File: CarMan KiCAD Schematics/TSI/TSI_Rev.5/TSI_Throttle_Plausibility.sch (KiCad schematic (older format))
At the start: 64 parts, among them Q2 MMBF170, SW1 TS5A3159DBVT, U16 TS372CDT, U18 MCP6004, U22 MCP23016-I_SO, U23 DAC5574IDGS, U3 TS912, U30 TLP293, U6 TS912, U7 MCP6004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

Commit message: TSI (~97%)
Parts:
- renumbered TP1 to APPS1_ISO1, TP2 to APPS1_b1, TP3 to APPS2_b1, TP9 to APPS_DIFF1
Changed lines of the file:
@@
 	2250 4250 2250 4550
 $Comp
-L Connector:TestPoint TP1
+L Connector:TestPoint APPS1_ISO1
 U 1 1 613A1566
 P 2250 4250
-F 0 "TP1" H 2308 4368 50  0000 L CNN
+F 0 "APPS1_ISO1" H 2308 4368 50  0000 L CNN
 F 1 "APPS1_ISO" H 2308 4277 50  0000 L CNN
 F 2 "TestPoint:TestPoint_Pad_D3.0mm" H 2450 4250 50  0001 C CNN
@@
 	6400 10350 6400 10150
 $Comp
-L Connector:TestPoint TP3
+L Connector:TestPoint APPS2_b1
 U 1 1 601142BC
 P 6400 10150
-F 0 "TP3" H 6458 10268 50  0000 L CNN
+F 0 "APPS2_b1" H 6458 10268 50  0000 L CNN
 F 1 "APPS2_b" H 6458 10177 50  0000 L CNN
 F 2 "TestPoint:TestPoint_Pad_D3.0mm" H 6600 10150 50  0001 C CNN
@@
 	3000 10350 3000 10150
 $Comp
-L Connector:TestPoint TP2
+L Connector:TestPoint APPS1_b1
 U 1 1 600FB539
 P 3000 10150
-F 0 "TP2" H 3058 10268 50  0000 L CNN
+F 0 "APPS1_b1" H 3058 10268 50  0000 L CNN
 F 1 "APPS1_b" H 3058 10177 50  0000 L CNN
 F 2 "TestPoint:TestPoint_Pad_D3.0mm" H 3200 10150 50  0001 C CNN
@@
 10V
 $Comp
-L Connector:TestPoint TP9
+L Connector:TestPoint APPS_DIFF1
 U 1 1 6003107E
 P 5400 1950
-F 0 "TP9" H 5200 2150 50  0000 L CNN
+F 0 "APPS_DIFF1" H 5200 2150 50  0000 L CNN
 F 1 "APPS_DIFF" H 5458 1977 50  0001 L CNN
 F 2 "TestPoint:TestPoint_Pad_D3.0mm" H 5600 1950 50  0001 C CNN

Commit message: TSI (~98.5%)
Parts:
- renumbered APPS1_ISO1 to TP1, APPS_DIFF1 to TP2, APPS1_b1 to TP3, APPS2_b1 to TP9
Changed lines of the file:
@@
 	2250 4250 2250 4550
 $Comp
-L Connector:TestPoint APPS1_ISO1
+L Connector:TestPoint TP1
 U 1 1 613A1566
 P 2250 4250
-F 0 "APPS1_ISO1" H 2308 4368 50  0000 L CNN
+F 0 "TP1" H 2308 4368 50  0000 L CNN
 F 1 "APPS1_ISO" H 2308 4277 50  0000 L CNN
 F 2 "TestPoint:TestPoint_Pad_D3.0mm" H 2450 4250 50  0001 C CNN
@@
 	6400 10350 6400 10150
 $Comp
-L Connector:TestPoint APPS2_b1
+L Connector:TestPoint TP9
 U 1 1 601142BC
 P 6400 10150
-F 0 "APPS2_b1" H 6458 10268 50  0000 L CNN
+F 0 "TP9" H 6458 10268 50  0000 L CNN
 F 1 "APPS2_b" H 6458 10177 50  0000 L CNN
 F 2 "TestPoint:TestPoint_Pad_D3.0mm" H 6600 10150 50  0001 C CNN
@@
 	3000 10350 3000 10150
 $Comp
-L Connector:TestPoint APPS1_b1
+L Connector:TestPoint TP3
 U 1 1 600FB539
 P 3000 10150
-F 0 "APPS1_b1" H 3058 10268 50  0000 L CNN
+F 0 "TP3" H 3058 10268 50  0000 L CNN
 F 1 "APPS1_b" H 3058 10177 50  0000 L CNN
 F 2 "TestPoint:TestPoint_Pad_D3.0mm" H 3200 10150 50  0001 C CNN
@@
 10V
 $Comp
-L Connector:TestPoint APPS_DIFF1
+L Connector:TestPoint TP2
 U 1 1 6003107E
 P 5400 1950
-F 0 "APPS_DIFF1" H 5200 2150 50  0000 L CNN
+F 0 "TP2" H 5350 2150 50  0000 L CNN
 F 1 "APPS_DIFF" H 5458 1977 50  0001 L CNN
 F 2 "TestPoint:TestPoint_Pad_D3.0mm" H 5600 1950 50  0001 C CNN

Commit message: Aesthetics
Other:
- note added: "*Need 1% tolerance for R17 & R18*\n"
- note removed: "*Need 1% tolerance for R27 & R28*\n"
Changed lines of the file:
@@
 Connection ~ 2150 6850
 Text Notes 1000 8150 0    50   ~ 0
-*Need 1% tolerance for R27 & R28*\n
+*Need 1% tolerance for R17 & R18*\n
 Text Label 2350 6850 0    50   ~ 0
 5V_REF

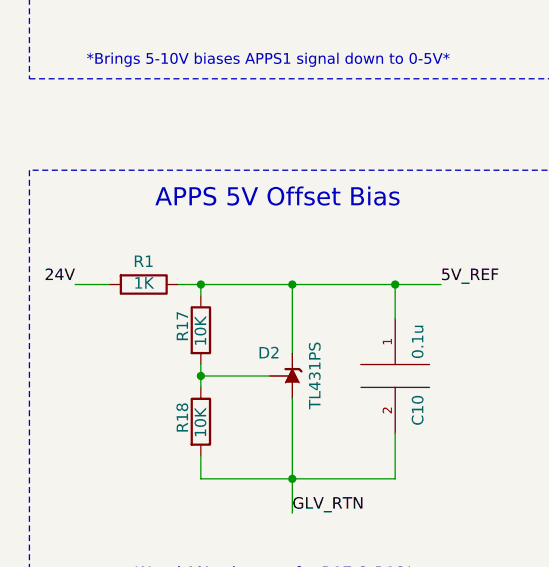
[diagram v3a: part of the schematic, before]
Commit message: Updated board, added silk art
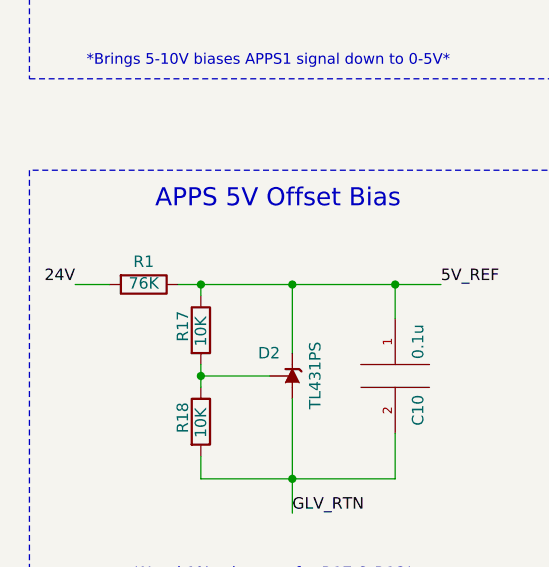
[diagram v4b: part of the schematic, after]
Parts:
- R1: value 1K -> 76K
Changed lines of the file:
@@
 P 1050 6850
 F 0 "R1" V 950 6850 50  0000 C CNN
-F 1 "1K" V 1074 6850 50  0000 C BNN
+F 1 "76K" V 1074 6850 50  0000 C BNN
 F 2 "Resistor_SMD:R_0805_2012Metric_Pad1.15x1.40mm_HandSolder" V 980 6850 50  0001 C CNN
 F 3 "~" H 1050 6850 50  0001 C CNN

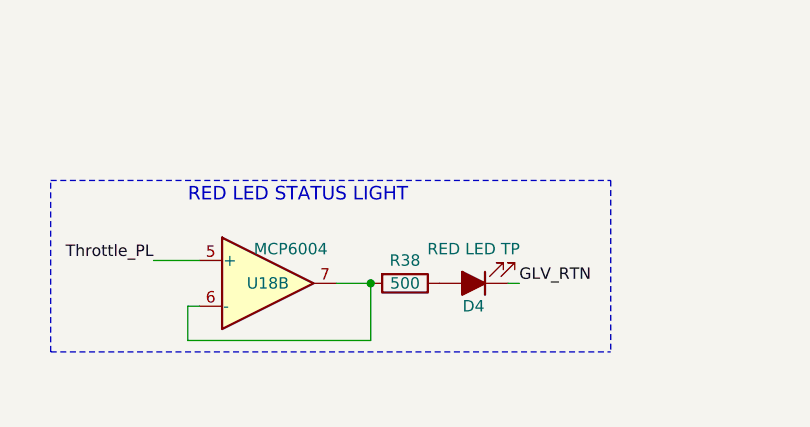
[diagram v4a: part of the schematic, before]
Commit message: Updated component links
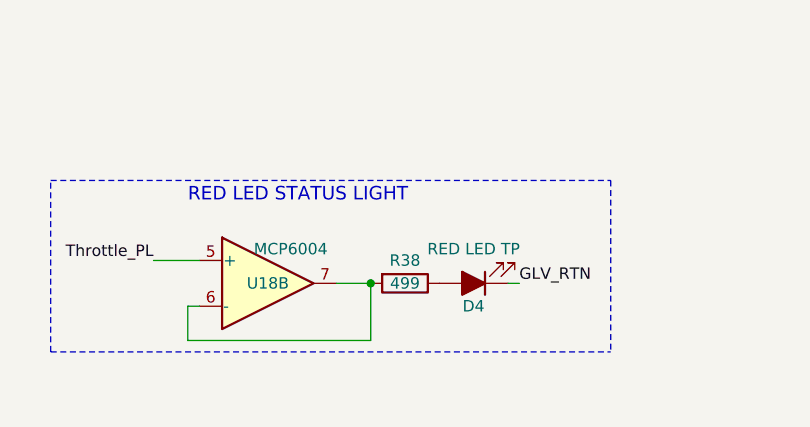
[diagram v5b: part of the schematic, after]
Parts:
- R38: value 500 -> 499
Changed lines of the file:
@@
 P 10000 10550
 F 0 "R38" V 9900 10550 50  0000 C CNN
-F 1 "500" V 10000 10550 50  0000 C CNN
+F 1 "499" V 10000 10550 50  0000 C CNN
 F 2 "Resistor_SMD:R_0805_2012Metric_Pad1.15x1.40mm_HandSolder" V 9930 10550 50  0001 C CNN
 F 3 "~" H 10000 10550 50  0001 C CNN

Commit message: Changed RV4 and RV5 footprint
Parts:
- RV4: footprint TSI_Rev_2021_Footprint_Lib:trim_pot -> TSI_Rev_2021_Footprint_Lib:Potentiometer
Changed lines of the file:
@@
 F 0 "RV4" H 5830 2246 50  0000 R CNN
 F 1 "1K" H 5830 2155 50  0000 R CNN
-F 2 "TSI_Rev_2021_Footprint_Lib:trim_pot" H 5900 2200 50  0001 C CNN
+F 2 "TSI_Rev_2021_Footprint_Lib:Potentiometer" H 5900 2200 50  0001 C CNN
 F 3 "~" H 5900 2200 50  0001 C CNN
 	1    5900 2200

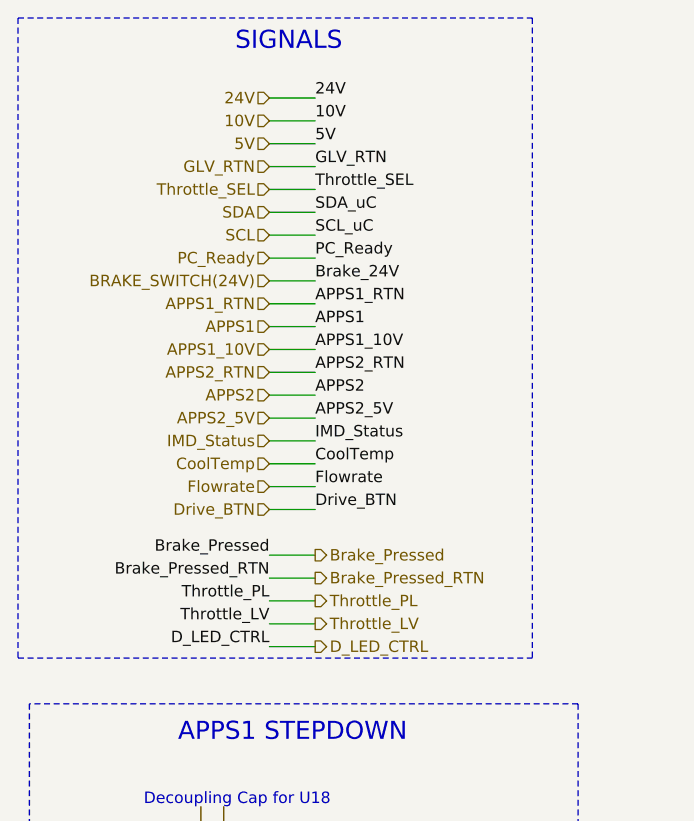
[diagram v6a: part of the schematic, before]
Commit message: TSI Signal Review ISSUES: - PCDC 'Pre_Charge_Ready' and 'PC_Ready' discrepancy - TSI Rev.4 IC1, IC4 -> PCDC & Isolators
REMOVED SIGNALS:
Throttle Plausibility
 - PC_Ready
 - Drive_BTN
 PCDC
 - HV+
 - HV-
 - Throttle_HV
 - IGNI_GND

STATUS LIGHTS & COCKPIT
- BP
- BP_RTN
- IMD_Status
- 5V
- Fault_LED
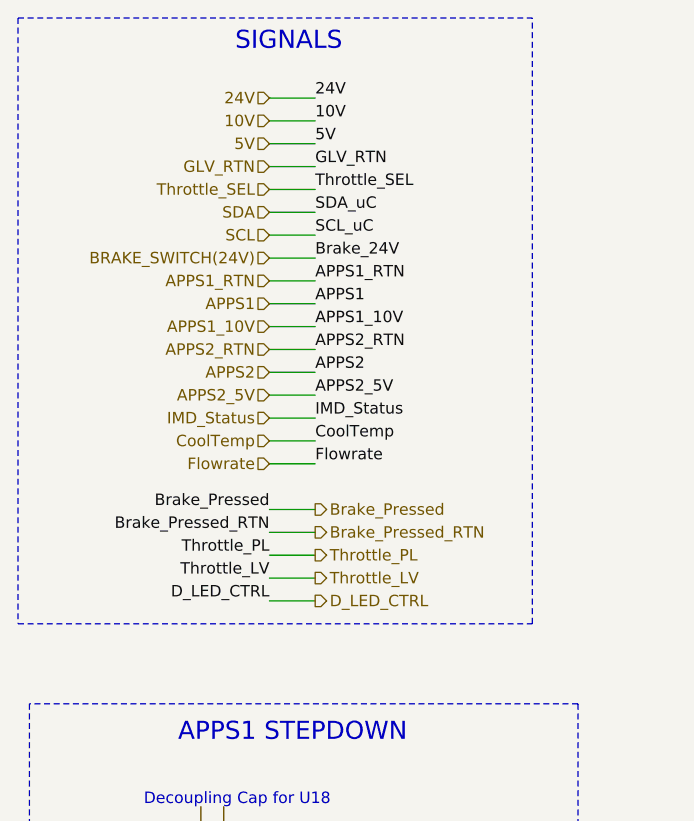
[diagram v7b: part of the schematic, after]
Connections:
- net labels removed: Drive_BTN, PC_Ready
- wire segments 288 -> 286
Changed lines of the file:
@@
 $Descr A3 16535 11693
 encoding utf-8
-Sheet 3 6
+Sheet 6 6
 Title ""
 Date ""
@@
 Text HLabel 1600 1450 0    50   Input ~ 0
 SCL
-Text HLabel 1600 1550 0    50   Input ~ 0
-PC_Ready
 Text Notes 1450 650  0    79   ~ 0
 SIGNALS\n
@@
 Text Label 1800 1050 0    50   ~ 0
 5V
-Wire Wire Line
-	1800 1550 1600 1550
-Text Label 1800 1550 0    50   ~ 0
-PC_Ready
 Wire Wire Line
 	2250 4250 2250 4550
@@
 Wire Wire Line
 	4100 2250 4250 2250
+Text Label 1800 1650 0    50   ~ 0
+APPS1_RTN
 Text Label 1800 1750 0    50   ~ 0
-APPS1_RTN
+APPS1
 Text Label 1800 1850 0    50   ~ 0
-APPS1
-Text Label 1800 1950 0    50   ~ 0
 APPS1_10V
+Text Label 1600 2750 2    50   ~ 0
+Brake_Pressed_RTN
+Text Label 1600 2650 2    50   ~ 0
+Brake_Pressed
+Wire Wire Line
+	1600 2750 1800 2750
+Wire Wire Line
+	1600 2650 1800 2650
 Text Label 1600 2950 2    50   ~ 0
+Throttle_LV
+Text Label 1600 2850 2    50   ~ 0
+Throttle_PL
+Wire Wire Line
+	1600 2950 1800 2950
+Wire Wire Line
+	1600 2850 1800 2850
+Text Label 1800 2050 0    50   ~ 0
+APPS2
+Text HLabel 1800 2850 2    50   Output ~ 0
+Throttle_PL
+Text HLabel 1800 2950 2    50   Output ~ 0
+Throttle_LV
+Text HLabel 1800 2750 2    50   Output ~ 0
 Brake_Pressed_RTN
-Text Label 1600 2850 2    50   ~ 0
-Brake_Pressed
-Wire Wire Line
-	1600 2950 1800 2950
-Wire Wire Line
-	1600 2850 1800 2850
-Text Label 1600 3150 2    50   ~ 0
-Throttle_LV
-Text Label 1600 3050 2    50   ~ 0
-Throttle_PL
-Wire Wire Line
-	1600 3150 1800 3150
-Wire Wire Line
-	1600 3050 1800 3050
-Text Label 1800 2150 0    50   ~ 0
-APPS2
-Text HLabel 1800 3050 2    50   Output ~ 0
-Throttle_PL
-Text HLabel 1800 3150 2    50   Output ~ 0
-Throttle_LV
-Text HLabel 1800 2950 2    50   Output ~ 0
-Brake_Pressed_RTN
-Text HLabel 1800 2850 2    50   Output ~ 0
+Text HLabel 1800 2650 2    50   Output ~ 0
 Brake_Pressed
 Wire Wire Line
@@
 Text Label 13050 8750 2    50   ~ 0
 24V
+Text HLabel 1600 1550 0    50   Input ~ 0
+BRAKE_SWITCH(24V)
+Text HLabel 1600 1750 0    50   Input ~ 0
+APPS1
 Text HLabel 1600 1650 0    50   Input ~ 0
-BRAKE_SWITCH(24V)
+APPS1_RTN
 Text HLabel 1600 1850 0    50   Input ~ 0
-APPS1
-Text HLabel 1600 1750 0    50   Input ~ 0
-APPS1_RTN
+APPS1_10V
 Text HLabel 1600 1950 0    50   Input ~ 0
-APPS1_10V
+APPS2_RTN
 Text HLabel 1600 2050 0    50   Input ~ 0
-APPS2_RTN
+APPS2
 Text HLabel 1600 2150 0    50   Input ~ 0
-APPS2
-Text HLabel 1600 2250 0    50   Input ~ 0
 APPS2_5V
 Wire Wire Line
+	1800 1750 1600 1750
+Wire Wire Line
+	1800 1550 1600 1550
+Wire Wire Line
+	1800 1950 1600 1950
+Wire Wire Line
 	1800 1850 1600 1850
 Wire Wire Line
+	1600 2050 1800 2050
+Wire Wire Line
 	1800 1650 1600 1650
 Wire Wire Line
-	1800 2050 1600 2050
-Wire Wire Line
-	1800 1950 1600 1950
-Wire Wire Line
-	1600 2150 1800 2150
-Wire Wire Line
-	1800 1750 1600 1750
-Wire Wire Line
-	1800 2250 1600 2250
+	1800 2150 1600 2150
 Wire Notes Line
 	2950 3500 550  3500
@@
 Wire Notes Line
 	2950 3500 2950 5950
-Text Label 1800 2050 0    50   ~ 0
+Text Label 1800 1950 0    50   ~ 0
 APPS2_RTN
-Text Label 1800 2250 0    50   ~ 0
+Text Label 1800 2150 0    50   ~ 0
 APPS2_5V
 Wire Notes Line
 	500  500  2750 500
-Wire Notes Line
-	500  3300 2750 3300
 Text Notes 12650 10350 0    157  ~ 0
 THROTTLE PLAUSIBILITY
@@
 Wire Wire Line
 	13300 3350 14150 3350
-Text HLabel 1600 2350 0    50   Input ~ 0
+Text HLabel 1600 2250 0    50   Input ~ 0
 IMD_Status
 Wire Wire Line
-	1600 2350 1800 2350
-Text Label 1800 2350 0    50   ~ 0
+	1600 2250 1800 2250
+Text Label 1800 2250 0    50   ~ 0
 IMD_Status
 Wire Wire Line
@@
 Wire Wire Line
 	10350 6100 10250 6100
-Text HLabel 1600 2450 0    50   Input ~ 0
+Text HLabel 1600 2350 0    50   Input ~ 0
 CoolTemp
 Wire Wire Line
-	1600 2450 1800 2450
-Text Label 1800 2450 0    50   ~ 0
+	1600 2350 1800 2350
+Text Label 1800 2350 0    50   ~ 0
 CoolTemp
 Text Label 10350 6200 0    50   ~ 0
@@
 Wire Wire Line
 	10250 6300 10350 6300
-Text HLabel 1800 3250 2    50   Output ~ 0
+Text HLabel 1800 3050 2    50   Output ~ 0
 D_LED_CTRL
-Text Label 1600 3250 2    50   ~ 0
+Text Label 1600 3050 2    50   ~ 0
 D_LED_CTRL
 Wire Wire Line
-	1600 3250 1800 3250
-Text HLabel 1600 2550 0    50   Input ~ 0
+	1600 3050 1800 3050
+Text HLabel 1600 2450 0    50   Input ~ 0
 Flowrate
 Wire Wire Line
-	1600 2550 1800 2550
-Text Label 1800 2550 0    50   ~ 0
+	1600 2450 1800 2450
+Text Label 1800 2450 0    50   ~ 0
 Flowrate
 Text Label 10350 6400 0    50   ~ 0
@@
 Wire Wire Line
 	10250 7000 10250 7100
-Text HLabel 1600 2650 0    50   Input ~ 0
-Drive_BTN
-Wire Wire Line
-	1600 2650 1800 2650
-Text Label 1800 2650 0    50   ~ 0
-Drive_BTN
 Wire Notes Line
 	16000 8250 16000 9900
-Wire Notes Line
-	2750 500  2750 3300
-Wire Notes Line
-	500  500  500  3300
 $Comp
 L Amplifier_Operational:MCP6004 U7
@@
 Wire Notes Line
 	12750 8250 16000 8250
-Text Label 1800 1650 0    50   ~ 0
+Text Label 1800 1550 0    50   ~ 0
 Brake_24V
 Text Label 13050 8600 0    50   ~ 0
@@
 	1    0    0    -1
 $EndComp
+Wire Notes Line
+	500  500  500  3150
+Wire Notes Line
+	500  3150 2750 3150
+Wire Notes Line
+	2750 3150 2750 500
 $EndSCHEMATC
